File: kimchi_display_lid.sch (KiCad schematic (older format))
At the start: 22 parts, among them J1 DF40HC(3.5)-60DS, J2 DF40HC(3.5)-60DS, J3 H19C-6S-0.5SH, J4 FH19C-40S-0.5SH(10), U1 24C32, U2 AP3019AKTR-G1

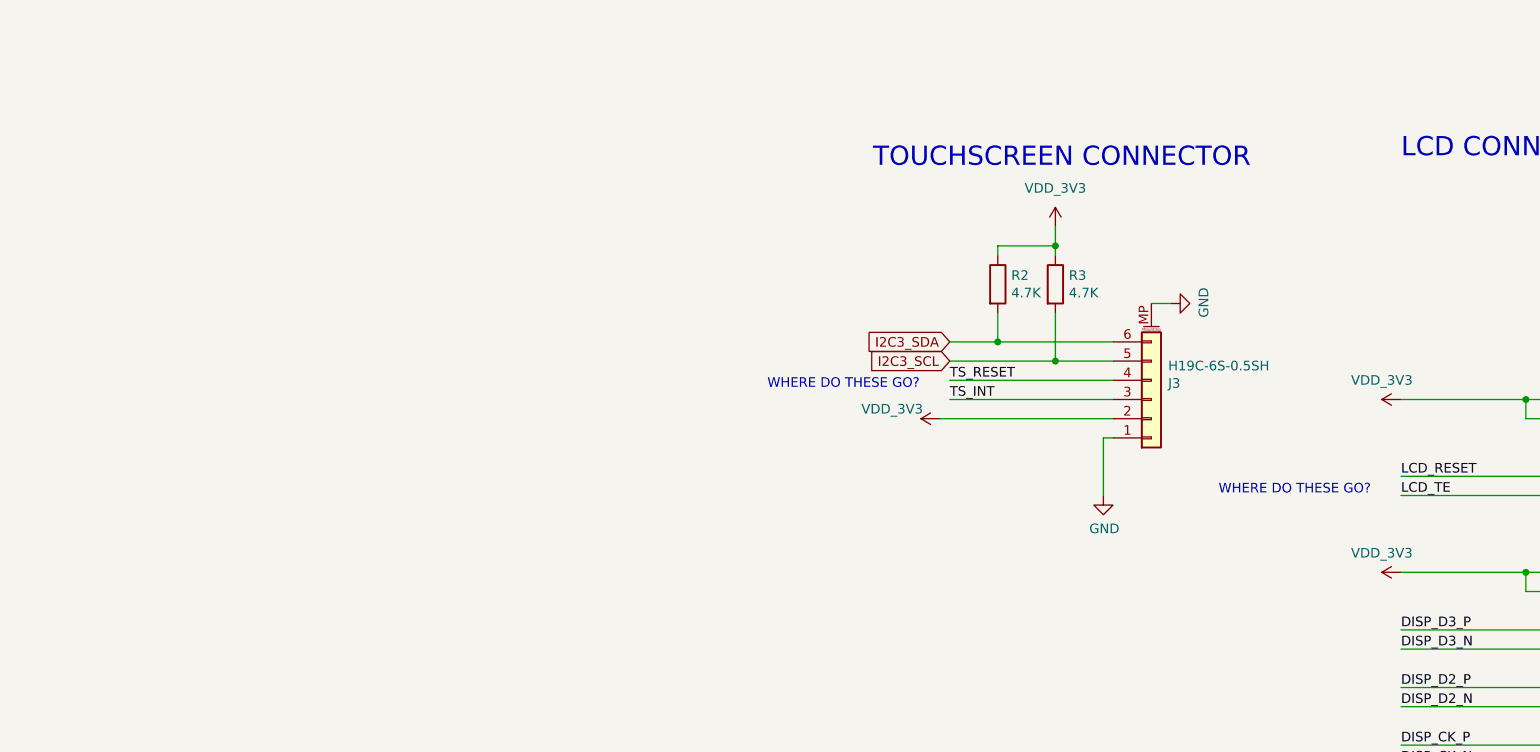
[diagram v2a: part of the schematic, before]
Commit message: Add level translator and route
Signed-off-by: Michael Welling <mwelling@ieee.org>
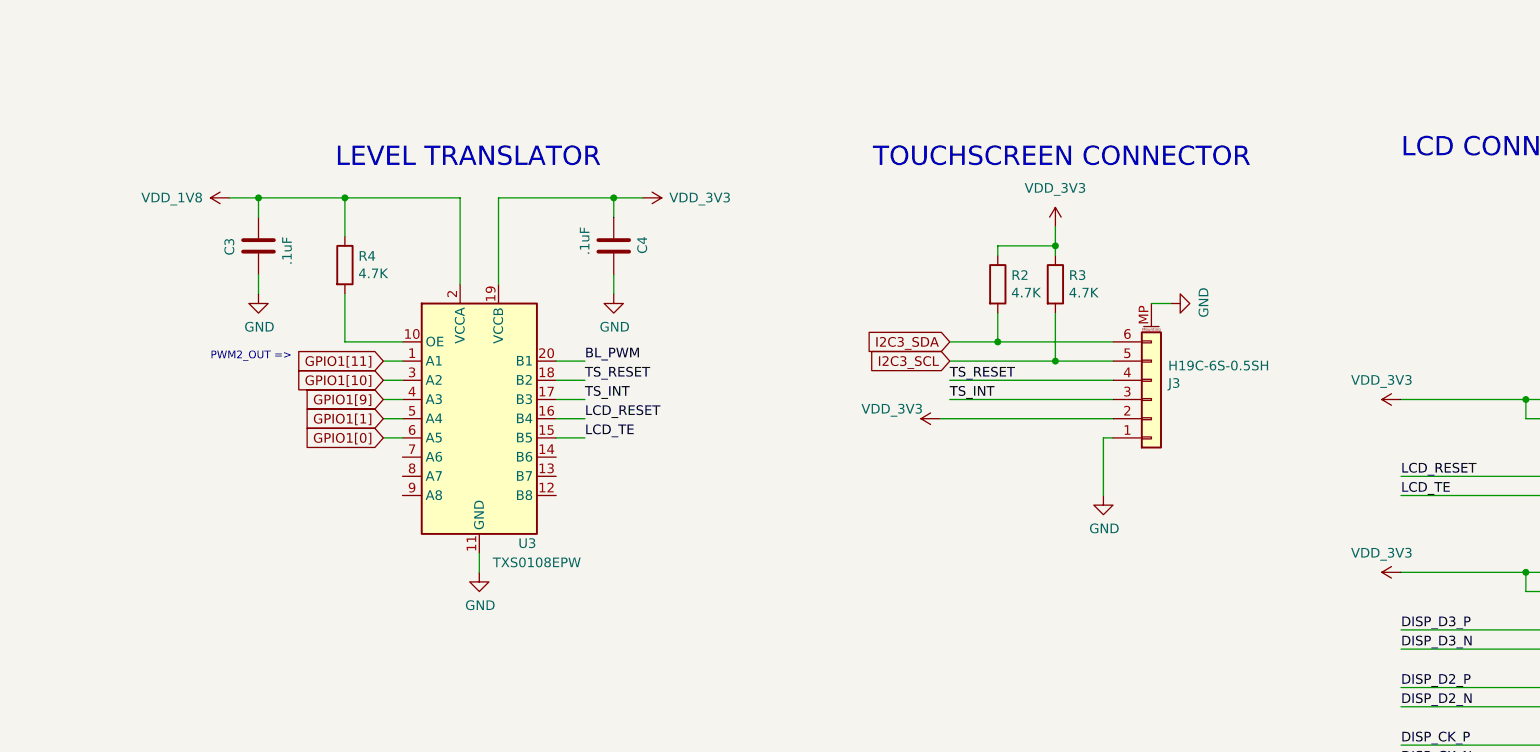
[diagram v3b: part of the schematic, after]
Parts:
- added C3, C4: .1uF, Capacitor_SMD:C_0603_1608Metric, symbol Device:C
- added R4: 4.7K, Resistor_SMD:R_0603_1608Metric, symbol Device:R
- added U3: TXS0108EPW, Package_SO:TSSOP-20_4.4x6.5mm_P0.65mm, symbol Logic_LevelTranslator:TXS0108EPW
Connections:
- net BL_PWM: now also U3.20 (B1)
- net GND: now also C3.2, C4.1, U3.11 (GND)
- net GPIO1[0]: now also U3.6 (A5)
- net GPIO1[10]: now also U3.3 (A2)
- net GPIO1[11]: now also U3.1 (A1)
- net GPIO1[1]: now also U3.5 (A4)
- net GPIO1[9]: now also U3.4 (A3)
- net LCD_RESET: now also U3.16 (B4)
- net LCD_TE: now also U3.15 (B5)
- net TS_INT: now also U3.17 (B3)
- net TS_RESET: now also U3.18 (B2)
- net VDD_1V8: now also C3.1, R4.1, U3.2 (VCCA)
- net VDD_3V3: now also C4.2, U3.19 (VCCB)
- new net: R4.2, U3.10 (OE)
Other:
- note added: "LEVEL TRANSLATOR"
- note added: "PWM2_OUT =>"
- note removed: "WHERE DO THESE GO?"
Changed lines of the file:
@@
 EESchema Schematic File Version 4
-LIBS:kimchi_display_lid-cache
-EELAYER 26 0
+EELAYER 30 0
 EELAYER END
 $Descr USLedger 17000 11000
@@
 	0    -1   -1   0
 $EndComp
-Text Notes 8500 7050 0    50   ~ 0
-WHERE DO THESE GO?
 Wire Wire Line
 	7950 6450 7100 6450
@@
 Wire Wire Line
 	7350 5800 7350 5750
-Text Notes 6150 6500 0    50   ~ 0
-WHERE DO THESE GO?
 Connection ~ 10100 9550
 Wire Wire Line
@@
 Text Notes 11050 6400 0    50   ~ 0
 NOTE: CONNECTORS INTENTIONALLY MIRRORED TO COMPENSATE\nFOR DIFFERENT PIN 1 CONVENTIONS ON THE CONNECTOR\nVERSUS THE FPC ON THE DISPLAY
+Text Label 5200 6350 0    50   ~ 0
+BL_PWM
+Text Label 5200 6450 0    50   ~ 0
+TS_RESET
+Text Label 5200 6550 0    50   ~ 0
+TS_INT
+Text Label 5200 6650 0    50   ~ 0
+LCD_RESET
+Text Label 5200 6750 0    50   ~ 0
+LCD_TE
+$Comp
+L Logic_LevelTranslator:TXS0108EPW U3
+U 1 1 5FE2117E
+P 4650 6650
+F 0 "U3" H 4900 6000 50  0000 C CNN
+F 1 "TXS0108EPW" H 4950 5900 50  0000 C CNN
+F 2 "Package_SO:TSSOP-20_4.4x6.5mm_P0.65mm" H 4650 5900 50  0001 C CNN
+F 3 "www.ti.com/lit/ds/symlink/txs0108e.pdf" H 4650 6550 50  0001 C CNN
+	1    4650 6650
+	1    0    0    -1
+$EndComp
+$Comp
+L power:GND #PWR07
+U 1 1 5FE24CFB
+P 4650 7450
+F 0 "#PWR07" H 4650 7200 50  0001 C CNN
+F 1 "GND" H 4655 7277 50  0000 C CNN
+F 2 "" H 4650 7450 50  0001 C CNN
+F 3 "" H 4650 7450 50  0001 C CNN
+	1    4650 7450
+	1    0    0    -1
+$EndComp
+Wire Wire Line
+	4650 7350 4650 7450
+$Comp
+L kimchi_ulid:VDD_3V3 #PWR08
+U 1 1 5FE2D407
+P 5500 5500
+F 0 "#PWR08" H 5500 5350 50  0001 C CNN
+F 1 "VDD_3V3" V 5500 5800 50  0000 C CNN
+F 2 "" H 5500 5500 50  0001 C CNN
+F 3 "" H 5500 5500 50  0001 C CNN
+	1    5500 5500
+	0    1    1    0
+$EndComp
+Wire Wire Line
+	5500 5500 5350 5500
+Wire Wire Line
+	5050 6350 5200 6350
+Wire Wire Line
+	5050 6450 5200 6450
+Wire Wire Line
+	5050 6550 5200 6550
+Wire Wire Line
+	5050 6650 5200 6650
+Wire Wire Line
+	5050 6750 5200 6750
+Text GLabel 4150 6550 0    50   Input ~ 0
+GPIO1[9]
+Text GLabel 4150 6350 0    50   Input ~ 0
+GPIO1[11]
+Text GLabel 4150 6750 0    50   Input ~ 0
+GPIO1[0]
+Text GLabel 4150 6650 0    50   Input ~ 0
+GPIO1[1]
+Text GLabel 4150 6450 0    50   Input ~ 0
+GPIO1[10]
+$Comp
+L kimchi_ulid:VDD_1V8 #PWR06
+U 1 1 5FE986B6
+P 3350 5500
+F 0 "#PWR06" H 3350 5350 50  0001 C CNN
+F 1 "VDD_1V8" V 3350 5800 50  0000 C CNN
+F 2 "" H 3350 5500 50  0001 C CNN
+F 3 "" H 3350 5500 50  0001 C CNN
+	1    3350 5500
+	0    -1   -1   0
+$EndComp
+Wire Wire Line
+	3350 5500 3500 5500
+$Comp
+L Device:C C4
+U 1 1 5FEAC292
+P 5350 5750
+F 0 "C4" V 5200 5700 50  0000 L CNN
+F 1 ".1uF" V 5500 5650 50  0000 L CNN
+F 2 "Capacitor_SMD:C_0603_1608Metric" H 5388 5600 50  0001 C CNN
+F 3 "~" H 5350 5750 50  0001 C CNN
+	1    5350 5750
+	-1   0    0    1
+$EndComp
+$Comp
+L Device:C C3
+U 1 1 5FEB58D2
+P 3500 5750
+F 0 "C3" V 3350 5700 50  0000 L CNN
+F 1 ".1uF" V 3650 5650 50  0000 L CNN
+F 2 "Capacitor_SMD:C_0603_1608Metric" H 3538 5600 50  0001 C CNN
+F 3 "~" H 3500 5750 50  0001 C CNN
+	1    3500 5750
+	1    0    0    -1
+$EndComp
+$Comp
+L power:GND #PWR09
+U 1 1 5FEB69BD
+P 5350 6000
+F 0 "#PWR09" H 5350 5750 50  0001 C CNN
+F 1 "GND" H 5355 5827 50  0000 C CNN
+F 2 "" H 5350 6000 50  0001 C CNN
+F 3 "" H 5350 6000 50  0001 C CNN
+	1    5350 6000
+	1    0    0    -1
+$EndComp
+Wire Wire Line
+	5350 5500 5350 5600
+Connection ~ 5350 5500
+Wire Wire Line
+	5350 5900 5350 6000
+$Comp
+L power:GND #PWR05
+U 1 1 5FEC56A6
+P 3500 6000
+F 0 "#PWR05" H 3500 5750 50  0001 C CNN
+F 1 "GND" H 3505 5827 50  0000 C CNN
+F 2 "" H 3500 6000 50  0001 C CNN
+F 3 "" H 3500 6000 50  0001 C CNN
+	1    3500 6000
+	1    0    0    -1
+$EndComp
+Wire Wire Line
+	3500 6000 3500 5900
+Wire Wire Line
+	3500 5600 3500 5500
+Connection ~ 3500 5500
+Wire Wire Line
+	4150 6350 4250 6350
+Wire Wire Line
+	4150 6450 4250 6450
+Wire Wire Line
+	4150 6550 4250 6550
+Wire Wire Line
+	4150 6650 4250 6650
+Wire Wire Line
+	4150 6750 4250 6750
+$Comp
+L Device:R R4
+U 1 1 5FF3952B
+P 3950 5850
+F 0 "R4" H 4020 5896 50  0000 L CNN
+F 1 "4.7K" H 4020 5805 50  0000 L CNN
+F 2 "Resistor_SMD:R_0603_1608Metric" V 3880 5850 50  0001 C CNN
+F 3 "~" H 3950 5850 50  0001 C CNN
+	1    3950 5850
+	1    0    0    -1
+$EndComp
+Wire Wire Line
+	4550 5500 4550 5950
+Wire Wire Line
+	3500 5500 3950 5500
+Wire Wire Line
+	3950 5700 3950 5500
+Connection ~ 3950 5500
+Wire Wire Line
+	3950 5500 4550 5500
+Wire Wire Line
+	4250 6250 3950 6250
+Wire Wire Line
+	3950 6250 3950 6000
+Wire Wire Line
+	4750 5500 4750 5950
+Wire Wire Line
+	4750 5500 5350 5500
+Text Notes 3900 5350 0    100  ~ 0
+LEVEL TRANSLATOR
+Text Notes 3250 6350 0    40   ~ 0
+PWM2_OUT =>
 $EndSCHEMATC

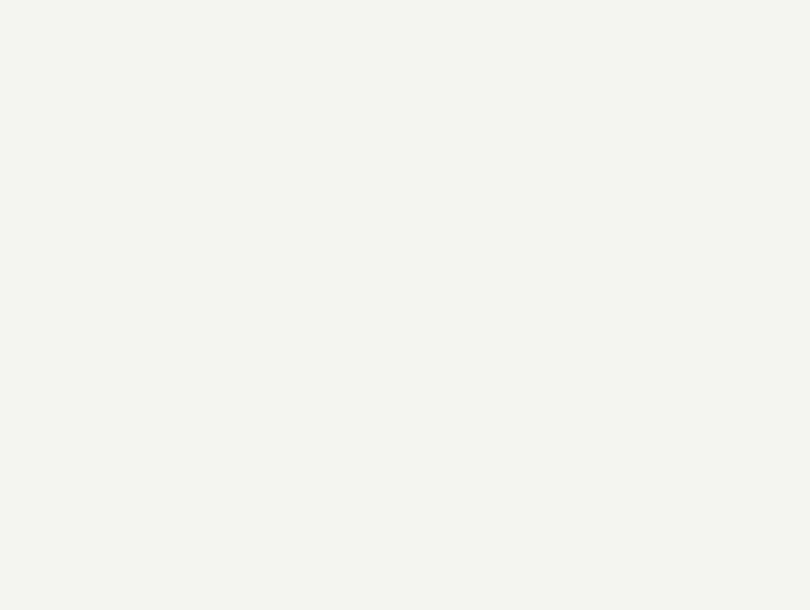
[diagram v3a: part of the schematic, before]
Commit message: Add USB connector
Signed-off-by: Michael Welling <mwelling@ieee.org>
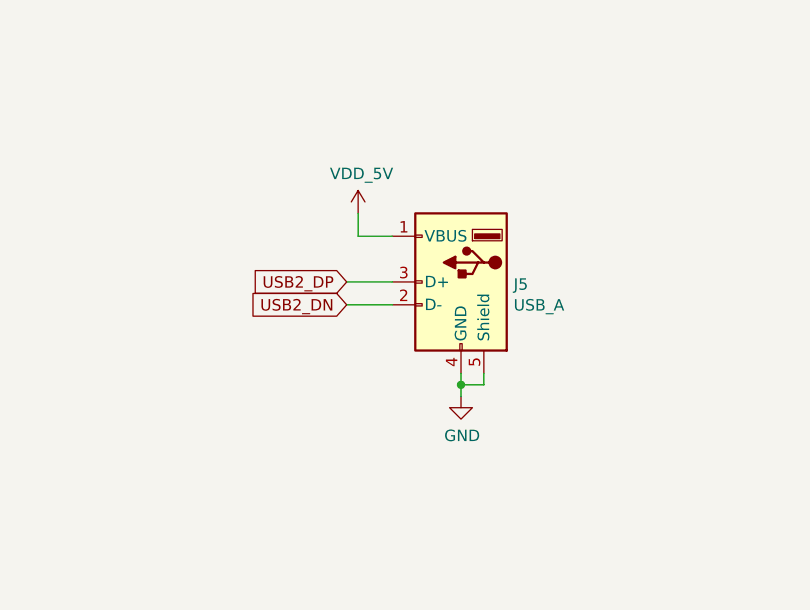
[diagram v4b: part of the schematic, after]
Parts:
- added J5: USB_A, kimchi_ulid:TE_1-292303-6, symbol Connector:USB_A
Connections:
- net GND: now also J5.4 (GND), J5.5 (Shield)
- net USB2_DN: now also J5.2 (D-)
- net USB2_DP: now also J5.3 (D+)
- net VDD_5V: now also J5.1 (VBUS)
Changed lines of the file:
@@
 Text Notes 3250 6350 0    40   ~ 0
 PWM2_OUT =>
+$Comp
+L Connector:USB_A J5
+U 1 1 6009A0A2
+P 14100 4450
+F 0 "J5" H 13870 4439 50  0000 R CNN
+F 1 "USB_A" H 13870 4348 50  0000 R CNN
+F 2 "kimchi_ulid:TE_1-292303-6" H 14250 4400 50  0001 C CNN
+F 3 " ~" H 14250 4400 50  0001 C CNN
+	1    14100 4450
+	-1   0    0    -1
+$EndComp
+$Comp
+L kimchi_ulid:VDD_5V #PWR0126
+U 1 1 6009E081
+P 13650 4150
+F 0 "#PWR0126" H 13650 4000 50  0001 C CNN
+F 1 "VDD_5V" H 13665 4323 50  0000 C CNN
+F 2 "" H 13650 4150 50  0001 C CNN
+F 3 "" H 13650 4150 50  0001 C CNN
+	1    13650 4150
+	1    0    0    -1
+$EndComp
+Text GLabel 13600 4550 0    50   Input ~ 0
+USB2_DN
+Text GLabel 13600 4450 0    50   Input ~ 0
+USB2_DP
+Wire Wire Line
+	13600 4450 13800 4450
+Wire Wire Line
+	13600 4550 13800 4550
+Wire Wire Line
+	13800 4250 13650 4250
+Wire Wire Line
+	13650 4250 13650 4150
+$Comp
+L power:GND #PWR0127
+U 1 1 600DC18C
+P 14100 4950
+F 0 "#PWR0127" H 14100 4700 50  0001 C CNN
+F 1 "GND" H 14105 4777 50  0000 C CNN
+F 2 "" H 14100 4950 50  0001 C CNN
+F 3 "" H 14100 4950 50  0001 C CNN
+	1    14100 4950
+	1    0    0    -1
+$EndComp
+Wire Wire Line
+	14100 4850 14100 4900
+Wire Wire Line
+	14100 4900 14200 4900
+Wire Wire Line
+	14200 4900 14200 4850
+Connection ~ 14100 4900
+Wire Wire Line
+	14100 4900 14100 4950
 $EndSCHEMATC

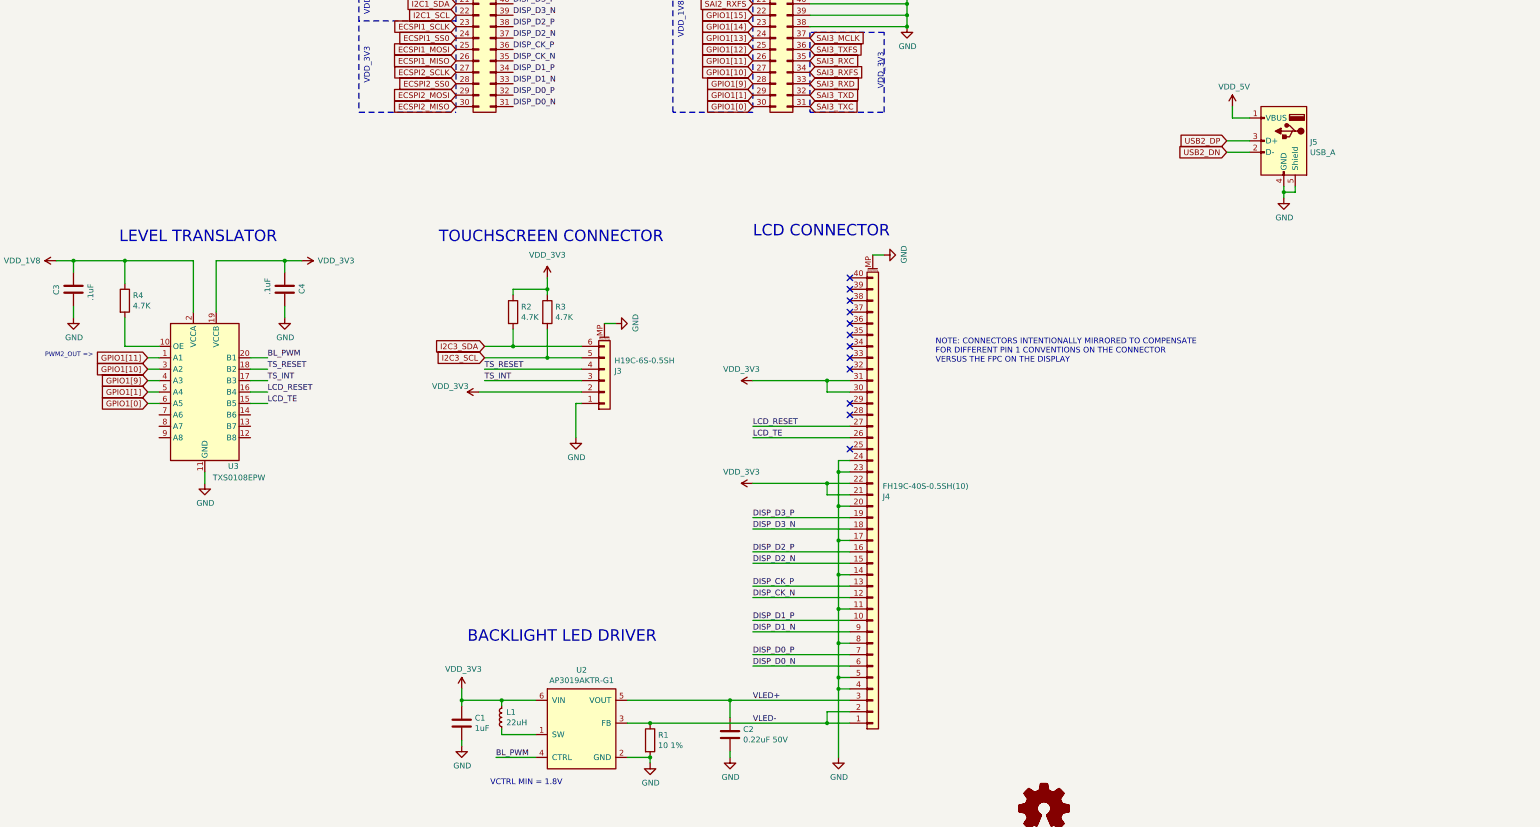
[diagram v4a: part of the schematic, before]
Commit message: Add 9DOF IMU
Signed-off-by: Michael Welling <mwelling@ieee.org>
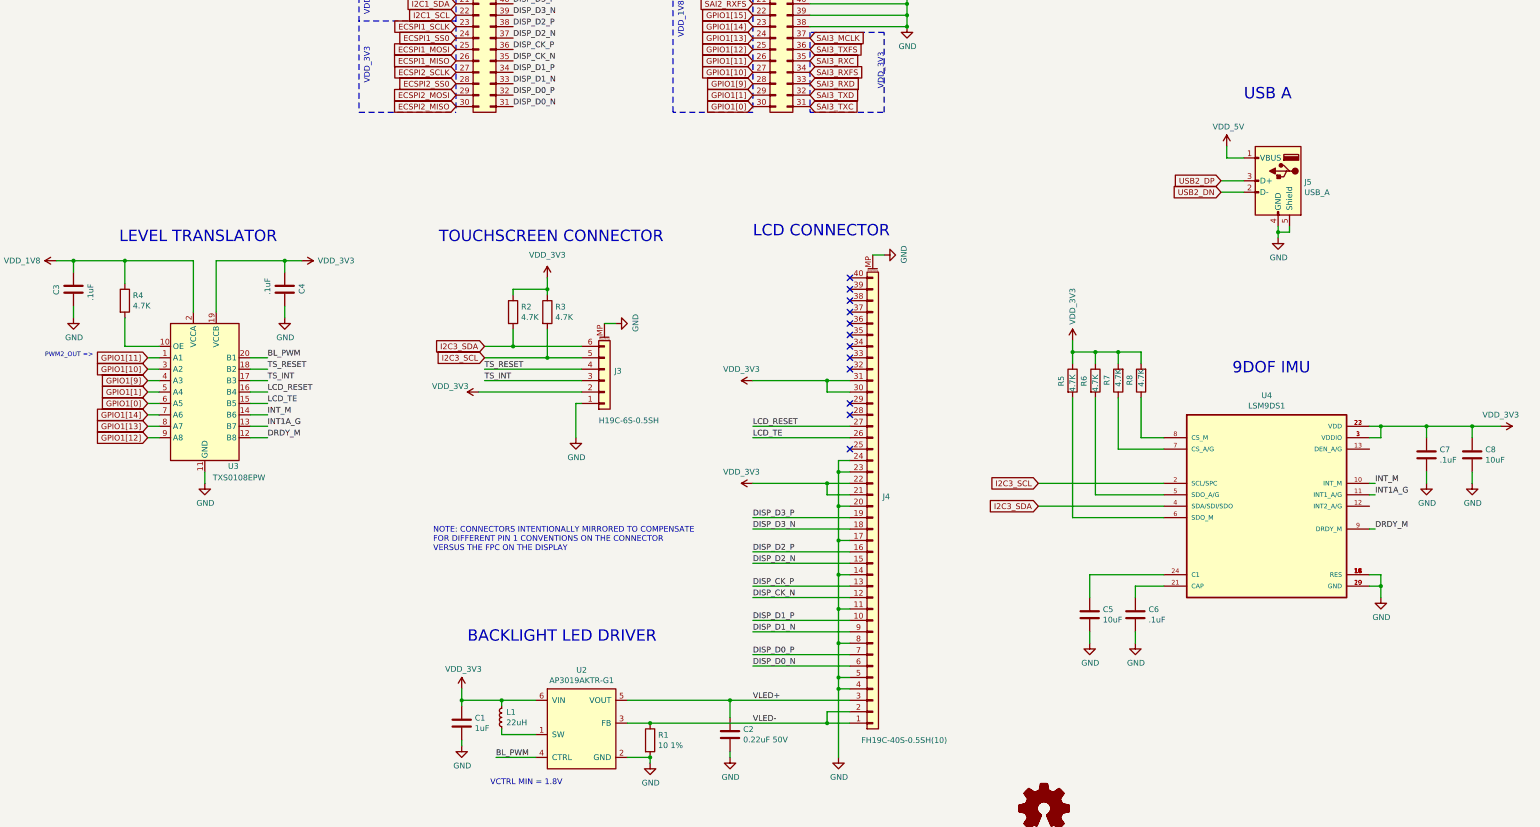
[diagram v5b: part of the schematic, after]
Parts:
- added C5, C8: 10uF, Capacitor_SMD:C_0603_1608Metric, symbol Device:C
- added C6, C7: .1uF, Capacitor_SMD:C_0603_1608Metric, symbol Device:C
- added R5, R6, R7, R8: 4.7K, Resistor_SMD:R_0603_1608Metric, symbol Device:R
- added U4: LSM9DS1, PQFN24P43_350X300X102L35X23N, symbol kimchi_ulid:LSM9DS1_LSM9DS1
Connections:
- net GND: now also C5.2, C6.2, C7.2, C8.2, U4.14 (RES), U4.15 (RES), U4.16 (RES), U4.17 (RES), U4.18 (RES), U4.19 (GND), U4.20 (GND)
- net GPIO1[12]: now also U3.9 (A8)
- net GPIO1[13]: now also U3.8 (A7)
- net GPIO1[14]: now also U3.7 (A6)
- net I2C3_SCL: now also U4.2 (SCL/SPC)
- net I2C3_SDA: now also U4.4 (SDA/SDI/SDO)
- net VDD_3V3: now also C7.1, C8.1, R5.1, R6.1, R7.2, R8.2, U4.1 (VDDIO), U4.22 (VDD), U4.23 (VDD), U4.3 (VDDIO)
- net DRDY_M: now reaches U3.12 (B8)
- net DRDY_M: now also U4.9 (DRDY_M)
- net INT1A_G: now reaches U3.13 (B7)
- net INT1A_G: now also U4.11 (INT1_A/G)
- net INT_M: now reaches U3.14 (B6)
- net INT_M: now also U4.10 (INT_M)
- new net: C6.1, U4.21 (CAP)
- new net: C5.1, U4.24 (C1)
- new net: R6.2, U4.5 (SDO_A/G)
- new net: R5.2, U4.6 (SDO_M)
- new net: R7.1, U4.7 (CS_A/G)
- new net: R8.1, U4.8 (CS_M)
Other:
- note added: "9DOF IMU"
- note added: "USB A"
- moved on the sheet: J5
